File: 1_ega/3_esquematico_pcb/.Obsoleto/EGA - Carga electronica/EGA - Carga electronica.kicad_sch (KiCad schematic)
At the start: 56 parts, among them J1 LCD20x4, J2 MCP4725, J3 ENCODER, J4 I2C1_Reservado, J5 UART0_Reservado, J6 V+, J7 Ventrada, J8 DS3231, Q1 IRFZ44, SW1 SW_Push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

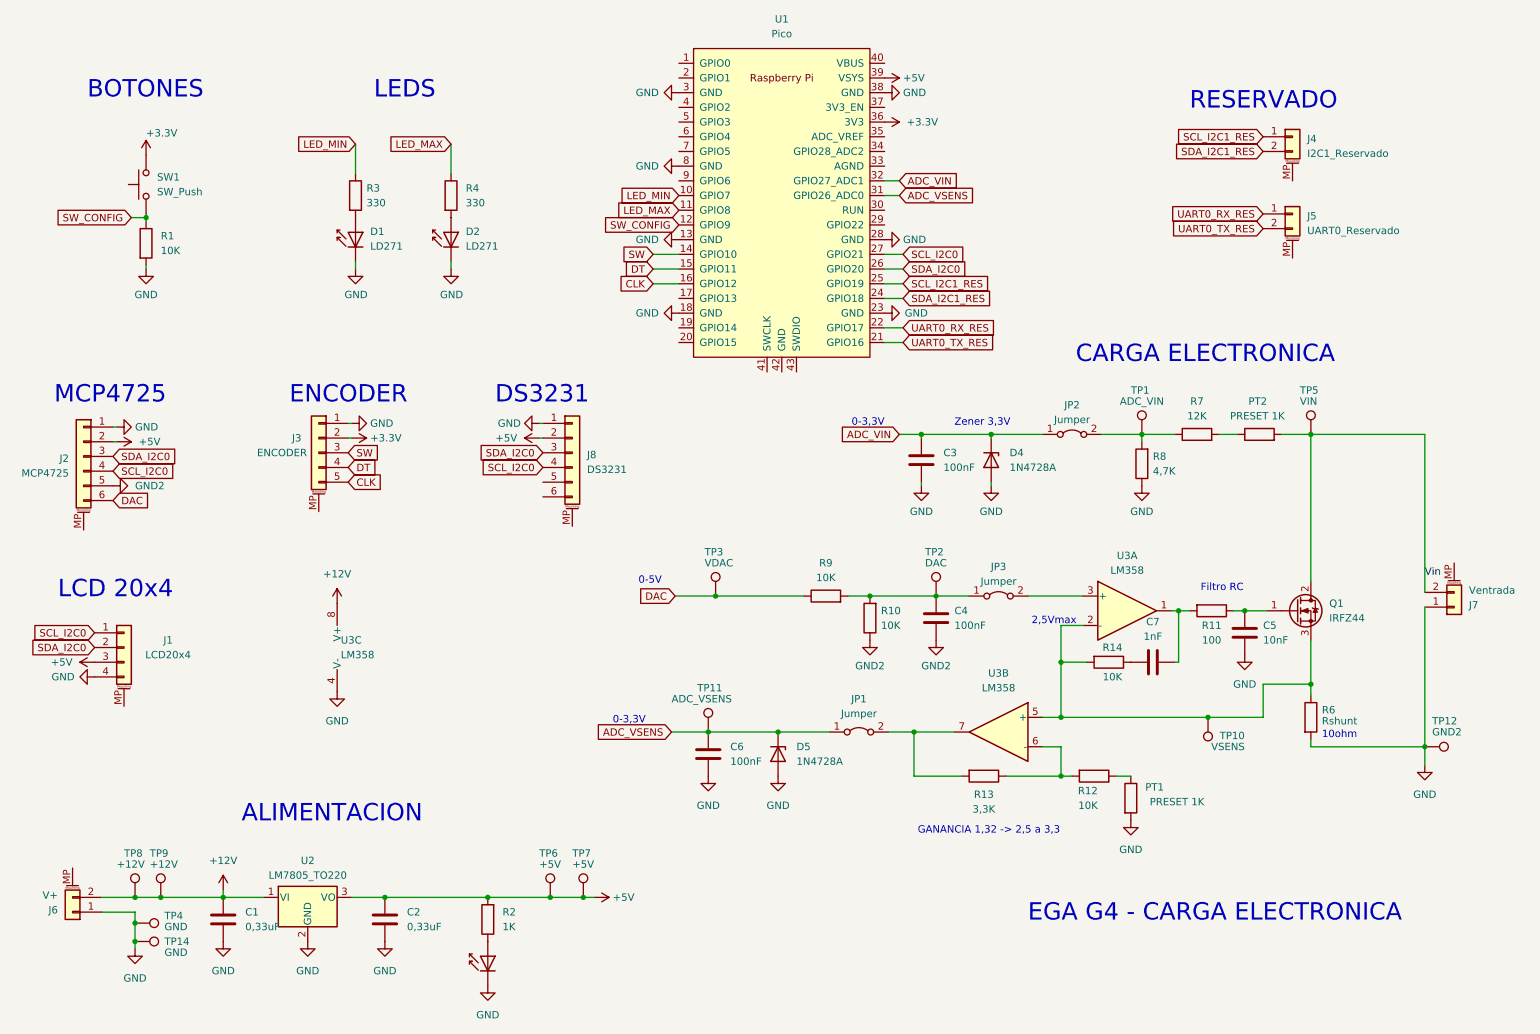
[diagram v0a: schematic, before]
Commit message: Se agrega task_Sensado
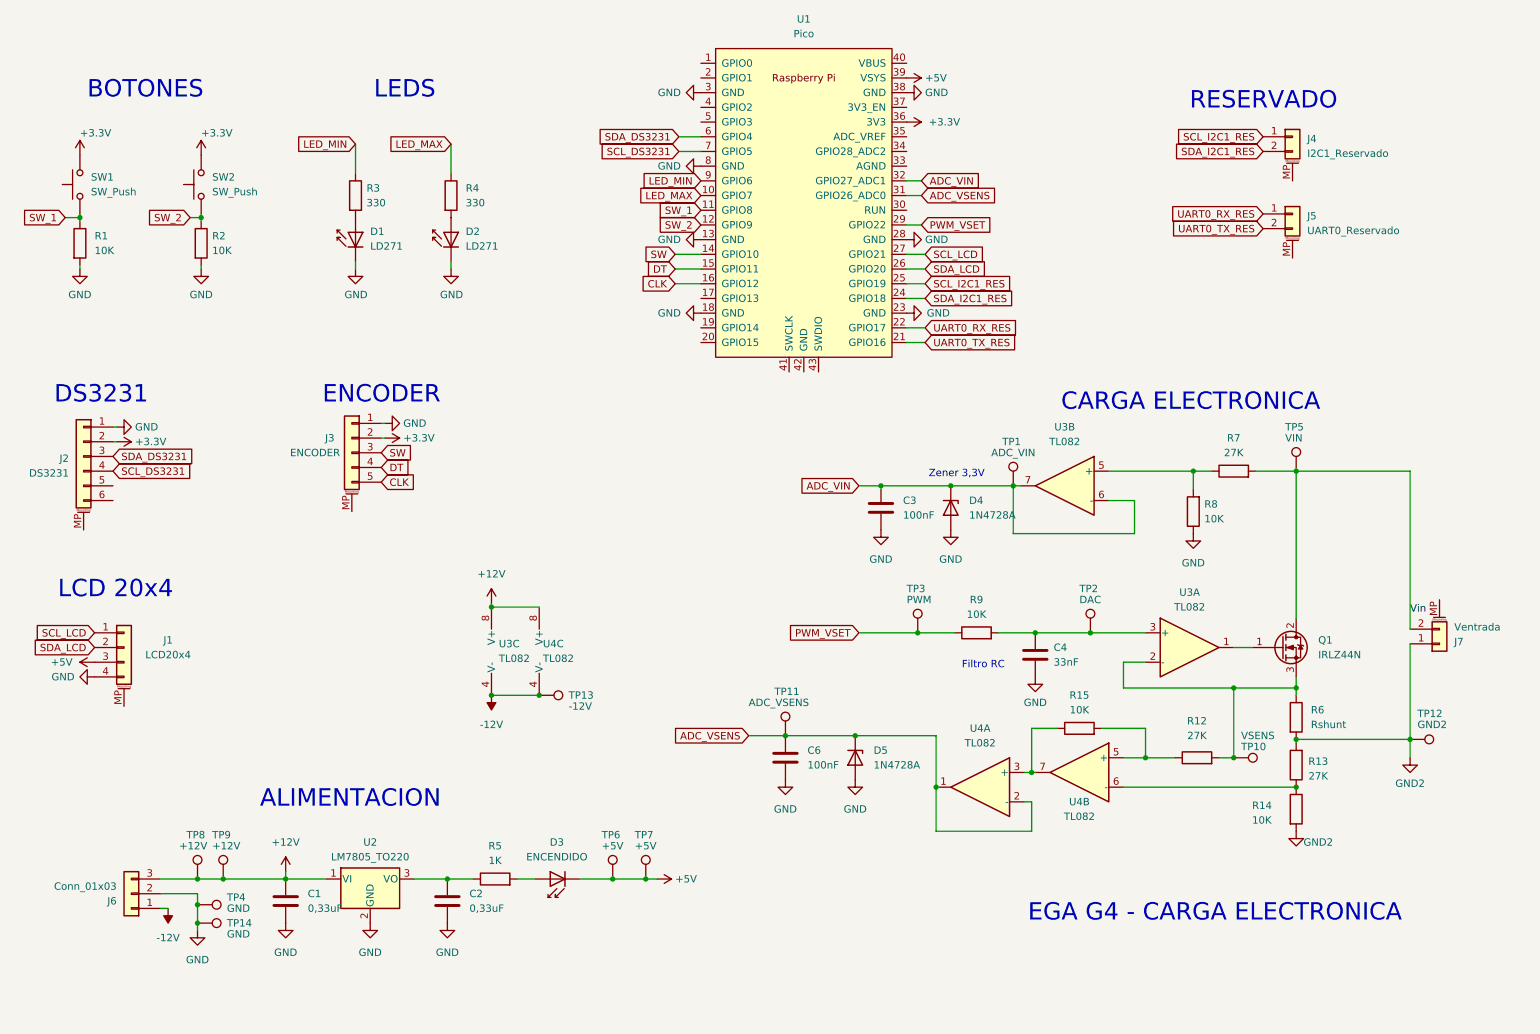
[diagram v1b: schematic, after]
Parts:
- removed C5: 10nF, Capacitor_THT:C_Disc_D7.0mm_W2.5mm_P5.00mm, symbol Device:C
- removed C7: 1nF, Capacitor_THT:C_Disc_D7.0mm_W2.5mm_P5.00mm, symbol Device:C
- removed J6: V+, TerminalBlock_Phoenix:TerminalBlock_Phoenix_MKDS-1,5-2-5.08_1x02_P5.08mm_Horizontal, symbol Connector_Generic_MountingPin:Conn_01x02_MountingPin
- removed J8: DS3231, Connector_PinHeader_2.54mm:PinHeader_1x06_P2.54mm_Vertical, symbol Connector_Generic_MountingPin:Conn_01x06_MountingPin
- removed JP1, JP2, JP3: Jumper, Connector_PinHeader_2.54mm:PinHeader_1x02_P2.54mm_Vertical, symbol Jumper:Jumper_2_Bridged
- removed PT1, PT2: PRESET 1K, Potentiometer_THT:Potentiometer_Piher_PT-10-V10_Vertical, symbol Device:R
- removed R10: 10K, Resistor_THT:R_Axial_DIN0207_L6.3mm_D2.5mm_P7.62mm_Horizontal, symbol Device:R
- removed R11: 100, Resistor_THT:R_Axial_DIN0207_L6.3mm_D2.5mm_P7.62mm_Horizontal, symbol Device:R
- removed U3: LM358, Package_DIP:DIP-8_W7.62mm_LongPads, symbol Amplifier_Operational:LM358
- added J6: Conn_01x03, TerminalBlock_Phoenix:TerminalBlock_Phoenix_MKDS-1,5-3-5.08_1x03_P5.08mm_Horizontal, symbol Connector_Generic:Conn_01x03
- added R15: 10K, Resistor_THT:R_Axial_DIN0207_L6.3mm_D2.5mm_P7.62mm_Horizontal, symbol Device:R
- added R5: 1K, Resistor_THT:R_Axial_DIN0207_L6.3mm_D2.5mm_P7.62mm_Horizontal, symbol Device:R
- added SW2: SW_Push, Button_Switch_THT:SW_PUSH_6mm_H5mm, symbol Switch:SW_Push
- added TP13: -12V, Connector_PinHeader_2.54mm:PinHeader_1x01_P2.54mm_Vertical, symbol Connector:TestPoint
- added U3, U4: TL082, Package_DIP:DIP-8_W7.62mm_Socket_LongPads, symbol Amplifier_Operational:TL082
- C4: value 100nF -> 33nF
- J2: value MCP4725 -> DS3231
- Q1: value IRFZ44 -> IRLZ44N
- R12: value 10K -> 27K
- R13: value 3,3K -> 27K
- R2: value 1K -> 10K
- R6: footprint Resistor_THT:R_Axial_DIN0414_L11.9mm_D4.5mm_P20.32mm_Horizontal -> Resistor_THT:R_Axial_DIN0414_L11.9mm_D4.5mm_P15.24mm_Horizontal
- R7: value 12K -> 27K
- R8: value 4,7K -> 10K
- TP3: value VDAC -> PWM
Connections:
- net +12V: now also J6.3 (Pin_3), U3.8 (V+), U4.8 (V+)
- net +3.3V: now also J2.2 (Pin_2), SW2.2
- net +5V: now also D3.1 (K); no longer C2.1, J2.2 (Pin_2), R2.2, U2.3 (VO)
- net ADC_VIN: now also TP1.1, U3.6 (-), U3.7
- net ADC_VSENS: now also U4.1, U4.2 (-)
- net GND: now also C4.2, R2.2, J6.2 (Pin_2); no longer D3.1 (K), J7.1 (Pin_1), R6.2, TP12.1
- net GND2: now also J7.1 (Pin_1), R13.2, R14.2, R6.2, TP12.1; no longer C4.2, J2.5 (Pin_5)
- net LED_MAX: now also U1.10 (GPIO7); no longer U1.11 (GPIO8)
- net LED_MIN: now also U1.9 (GPIO6); no longer U1.10 (GPIO7)
- net Vin: now also R7.2
- net at C4.1, R9.2, TP2.1: now also U3.3 (+)
- net at R12.2: now also Q1.3 (S), R6.1, TP10.1, U3.2 (-); no longer R13.1
- net at D3.2 (A): now also R5.2; no longer R2.1
- net at R12.1: now also R15.2, U4.5 (+)
- net at R7.1, R8.2: now also U3.5 (+); no longer TP1.1
- net at R14.1: now also R13.1, U4.6 (-)
- net at Q1.1 (G): now also U3.1
- net PWM_VSET: now reaches U1.29 (GPIO22)
- net PWM_VSET: now also R9.1, TP3.1
- net SDA_DS3231: now reaches U1.6 (GPIO4)
- net SDA_DS3231: now also J2.3 (Pin_3)
- net SCL_DS3231: now reaches U1.7 (GPIO5)
- net SCL_DS3231: now also J2.4 (Pin_4)
- removed net DAC: J2.6 (Pin_6), R9.1, TP3.1
- net SCL_I2C0 renamed SCL_LCD
- net SCL_LCD: no longer J2.4 (Pin_4)
- net SDA_I2C0 renamed SDA_LCD
- net SDA_LCD: no longer J2.3 (Pin_3)
- net SW_CONFIG renamed SW_1
- net SW_1: now also U1.11 (GPIO8); no longer U1.12 (GPIO9)
- new net: R15.1, U4.3 (+), U4.7
- new net: C2.1, R5.1, U2.3 (VO)
- new net -12V: J6.1 (Pin_1), TP13.1, U3.4 (V-), U4.4 (V-)
- new net SW_2: R2.1, SW2.1, U1.12 (GPIO9)
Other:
- note removed: "0-3,3V"
- note removed: "0-5V"
- note removed: "10ohm"
- note removed: "2,5Vmax"
- note removed: "GANANCIA 1,32 -> 2,5 a 3,3"
- note removed: "MCP4725"
- moved on the sheet: C1, C2, C3, C4, C6, D4, D5, J3, J7, Q1, R1, R6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
